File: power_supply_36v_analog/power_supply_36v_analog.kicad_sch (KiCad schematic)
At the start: 0 parts

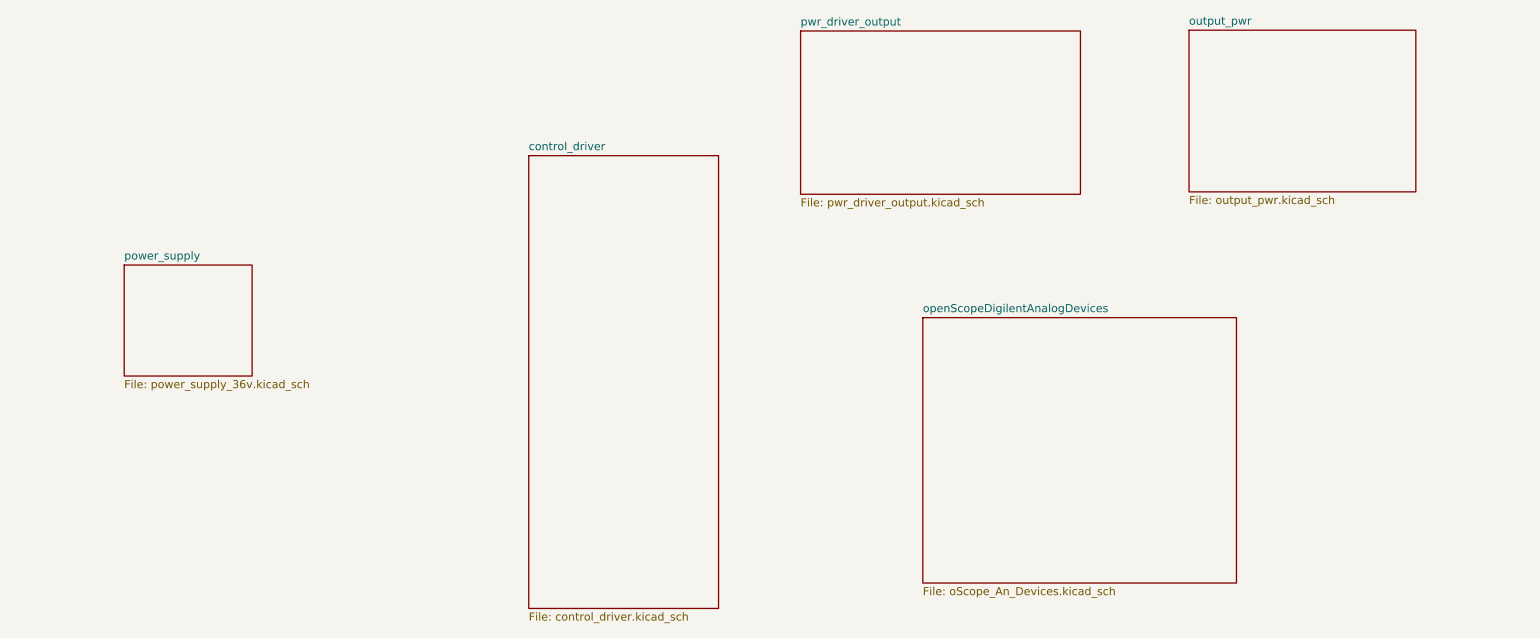
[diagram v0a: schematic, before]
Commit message: Convert global labels to hierarchical pins in all schematic sheets
- control_driver.kicad_sch: US-, output_U-, to_base_driver_adjust, NODO_001, U-
- pwr_driver_output.kicad_sch: AMPERIMETRO+, to_base_driver_adjust, NODO_001, U+
- output_pwr.kicad_sch: U+, V-, U-, output_U-
- power_supply_36v.kicad_sch: TR21, +36V, TR11, TR12, TR22, -36V
- Added corresponding pins to sheet symbols in root schematic
- Updated .gitignore to exclude .history and .lck files
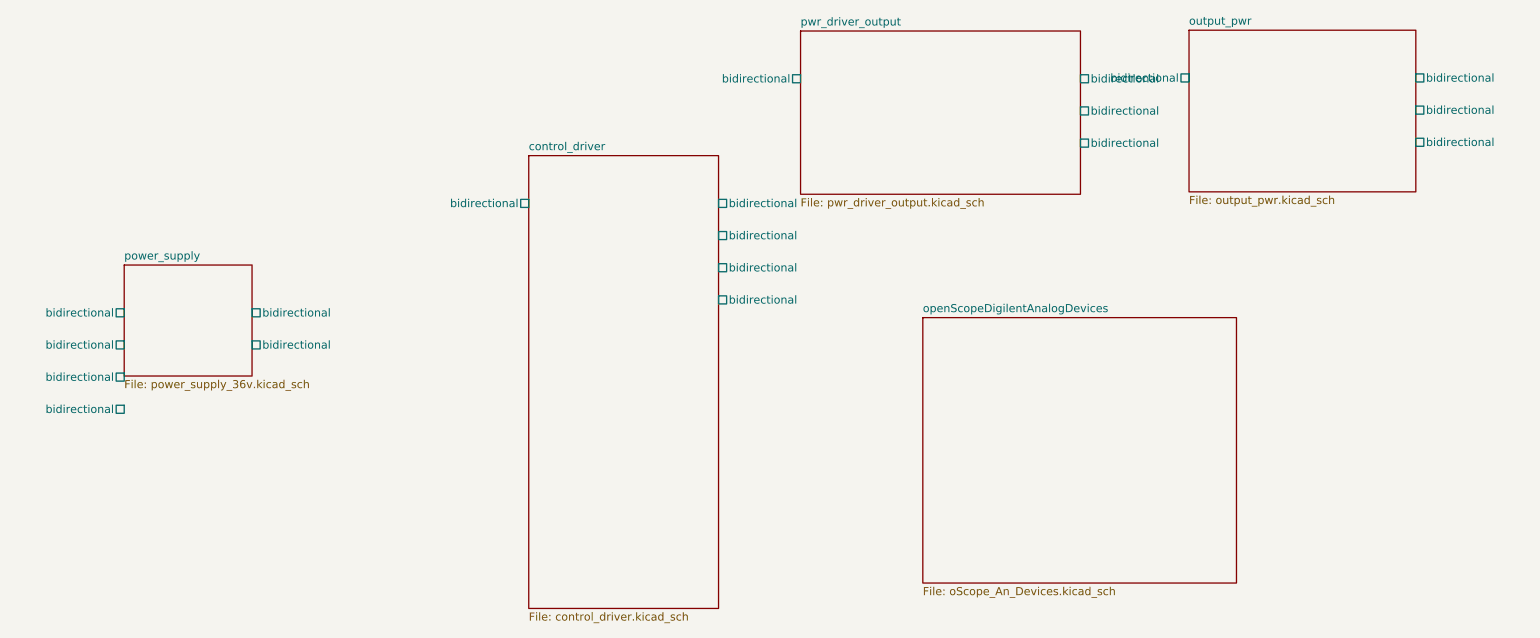
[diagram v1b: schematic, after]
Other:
- sheet control_driver ports: added bidirectional; removed none
- sheet output_pwr ports: added bidirectional; removed none
- sheet power_supply ports: added bidirectional; removed none
- sheet pwr_driver_output ports: added bidirectional; removed none
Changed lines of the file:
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@@
       )
+    )
+    (pin bidirectional line
+      (at 58.293 93.27 0)
+      (length 2.54)
+      (name "TR21" (effects (font (size 1.27 1.27))))
+    )
+    (pin bidirectional line
+      (at 58.293 98.34 0)
+      (length 2.54)
+      (name "TR11" (effects (font (size 1.27 1.27))))
+    )
+    (pin bidirectional line
+      (at 58.293 103.42 0)
+      (length 2.54)
+      (name "TR12" (effects (font (size 1.27 1.27))))
+    )
+    (pin bidirectional line
+      (at 58.293 108.50 0)
+      (length 2.54)
+      (name "TR22" (effects (font (size 1.27 1.27))))
+    )
+    (pin bidirectional line
+      (at 78.49 93.27 180)
+      (length 2.54)
+      (name "+36V" (effects (font (size 1.27 1.27))))
+    )
+    (pin bidirectional line
+      (at 78.49 98.34 180)
+      (length 2.54)
+      (name "-36V" (effects (font (size 1.27 1.27))))
     )
   )
@@
       )
     )
+    (pin bidirectional line
+      (at 226.441 56.18 0)
+      (length 2.54)
+      (name "output_U-" (effects (font (size 1.27 1.27))))
+    )
+    (pin bidirectional line
+      (at 262.25 56.18 180)
+      (length 2.54)
+      (name "U+" (effects (font (size 1.27 1.27))))
+    )
+    (pin bidirectional line
+      (at 262.25 61.26 180)
+      (length 2.54)
+      (name "V-" (effects (font (size 1.27 1.27))))
+    )
+    (pin bidirectional line
+      (at 262.25 66.34 180)
+      (length 2.54)
+      (name "U-" (effects (font (size 1.27 1.27))))
+    )
   )
   (sheet (at 165.1 48.768) (size 44.196 25.781) (fields_autoplaced)
@@
         (path "/30614b12-2e70-4eaa-ab37-37bf81f07fd3" (page "3"))
       )
+    )
+    (pin bidirectional line
+      (at 165.1 56.31 0)
+      (length 2.54)
+      (name "AMPERIMETRO+" (effects (font (size 1.27 1.27))))
+    )
+    (pin bidirectional line
+      (at 209.30 56.31 180)
+      (length 2.54)
+      (name "to_base_driver_adjust" (effects (font (size 1.27 1.27))))
+    )
+    (pin bidirectional line
+      (at 209.30 61.39 180)
+      (length 2.54)
+      (name "NODO_001" (effects (font (size 1.27 1.27))))
+    )
+    (pin bidirectional line
+      (at 209.30 66.47 180)
+      (length 2.54)
+      (name "U+" (effects (font (size 1.27 1.27))))
     )
   )
@@
       )
     )
+    (pin bidirectional line
+      (at 122.174 75.99 0)
+      (length 2.54)
+      (name "US-" (effects (font (size 1.27 1.27))))
+    )
+    (pin bidirectional line
+      (at 152.15 75.99 180)
+      (length 2.54)
+      (name "output_U-" (effects (font (size 1.27 1.27))))
+    )
+    (pin bidirectional line
+      (at 152.15 81.07 180)
+      (length 2.54)
+      (name "to_base_driver_adjust" (effects (font (size 1.27 1.27))))
+    )
+    (pin bidirectional line
+      (at 152.15 86.15 180)
+      (length 2.54)
+      (name "NODO_001" (effects (font (size 1.27 1.27))))
+    )
+    (pin bidirectional line
+      (at 152.15 91.23 180)
+      (length 2.54)
+      (name "U-" (effects (font (size 1.27 1.27))))
+    )
   )
